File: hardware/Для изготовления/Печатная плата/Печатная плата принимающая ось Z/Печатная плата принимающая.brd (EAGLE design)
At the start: 30.4 x 29.2 mm, 6 parts, among them J1 22-03-5035, X1 0446200001

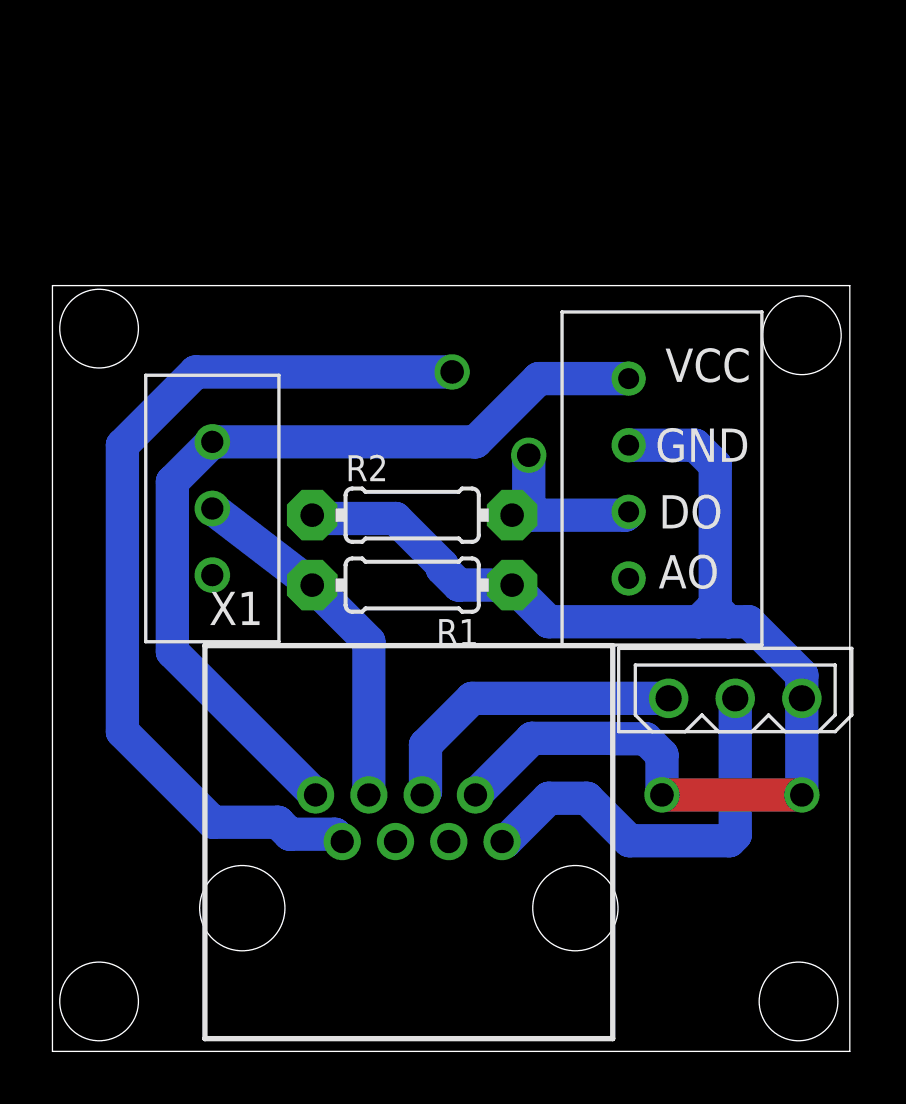
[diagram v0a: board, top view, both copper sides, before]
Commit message: Изменена плата принимающая под  ось Z
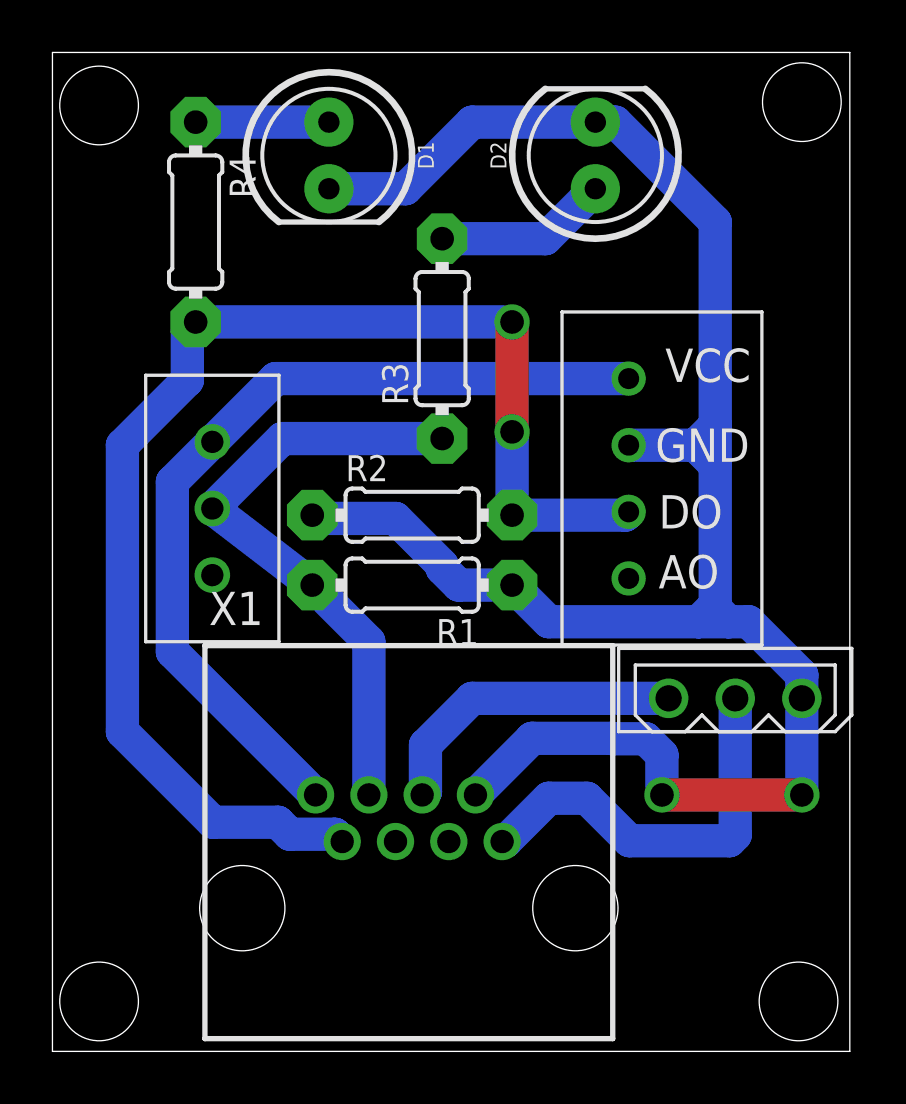
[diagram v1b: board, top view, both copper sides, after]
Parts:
- added D1, D2: (no value), SparkFun-LED:LED_5MM
- added R3, R4: (no value), resistor:0204/7
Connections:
- new net N$1: D2.A, R3.2
- new net N$2: D1.A, R4.1
- net ENCODER: now also R4.2
- net ENDSTOP: now also R3.1
- net GND: now also D1.K, D2.K
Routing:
- net GND: track 51.7 -> 79.4 mm
- net ENDSTOP: track 13.7 -> 23.6 mm
- net ENCODER: track 41.6 -> 50.8 mm
- net N$1: track 0.00 -> 6.63 mm
- net N$2: track 0.00 -> 5.08 mm
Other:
- board size 30.4 x 29.2 mm -> 30.4 x 38.1 mm
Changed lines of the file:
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@@
 <layer number="230" name="230bmp" color="7" fill="1" visible="yes" active="yes"/>
 <layer number="231" name="231bmp" color="7" fill="1" visible="yes" active="yes"/>
+<layer number="232" name="Eagle3D_PG2" color="7" fill="1" visible="yes" active="yes"/>
+<layer number="233" name="Eagle3D_PG3" color="7" fill="1" visible="yes" active="yes"/>
 <layer number="248" name="Housing" color="7" fill="1" visible="yes" active="yes"/>
 <layer number="249" name="Edge" color="7" fill="1" visible="yes" active="yes"/>
@@
 <plain>
 <wire x1="16.129" y1="-1.143" x2="46.533" y2="-1.143" width="0" layer="20"/>
-<wire x1="46.533" y1="-1.143" x2="46.533" y2="28.057" width="0" layer="20"/>
-<wire x1="46.533" y1="28.057" x2="16.129" y2="28.057" width="0" layer="20"/>
-<wire x1="16.129" y1="28.057" x2="16.129" y2="-1.143" width="0" layer="20"/>
-<hole x="17.907" y="26.416" drill="3"/>
+<wire x1="46.533" y1="-1.143" x2="46.533" y2="36.947" width="0" layer="20"/>
+<wire x1="46.533" y1="36.947" x2="16.129" y2="36.947" width="0" layer="20"/>
+<wire x1="16.129" y1="36.947" x2="16.129" y2="-1.143" width="0" layer="20"/>
+<hole x="17.907" y="34.925" drill="3"/>
 <hole x="17.907" y="0.762" drill="3"/>
 <hole x="44.577" y="0.762" drill="3"/>
-<hole x="44.704" y="26.162" drill="3"/>
+<hole x="44.704" y="35.052" drill="3"/>
 </plain>
 <attributes>
@@
 <attribute name="OC_FARNELL" value="unknown" x="29.718" y="4.318" size="1.778" layer="27" display="off"/>
 </element>
+<element name="D1" library="SparkFun-LED" package="LED_5MM" value="" x="26.67" y="33.02" rot="R270"/>
+<element name="D2" library="SparkFun-LED" package="LED_5MM" value="" x="36.83" y="33.02" rot="R90"/>
+<element name="R3" library="resistor" library_urn="urn:adsk.eagle:library:348" package="0204/7" package3d_urn="urn:adsk.eagle:package:25945/1" value="" x="30.988" y="26.035" rot="R90"/>
+<element name="R4" library="resistor" library_urn="urn:adsk.eagle:library:348" package="0204/7" package3d_urn="urn:adsk.eagle:package:25945/1" value="" x="21.59" y="30.48" rot="R270"/>
 </elements>
 <signals>
@@
 <contactref element="U$1" pad="VCC"/>
 <contactref element="U$2" pad="NC"/>
-<wire x1="38.1" y1="24.511" x2="34.671" y2="24.511" width="1.27" layer="16"/>
-<wire x1="32.258" y1="22.098" x2="22.225" y2="22.098" width="1.27" layer="16"/>
-<wire x1="34.671" y1="24.511" x2="32.258" y2="22.098" width="1.27" layer="16"/>
 <contactref element="X1" pad="8"/>
 <wire x1="22.225" y1="22.098" x2="20.701" y2="20.574" width="1.27" layer="16"/>
 <wire x1="20.701" y1="14.097" x2="26.162" y2="8.636" width="1.27" layer="16"/>
 <wire x1="20.701" y1="20.574" x2="20.701" y2="14.097" width="1.27" layer="16"/>
+<wire x1="22.225" y1="22.098" x2="24.638" y2="24.511" width="1.27" layer="16"/>
+<wire x1="24.638" y1="24.511" x2="38.1" y2="24.511" width="1.27" layer="16"/>
 </signal>
 <signal name="GND">
@@
 <wire x1="37.4824" y1="10.7776" x2="38.7524" y2="10.7776" width="1.27" layer="16"/>
 <wire x1="38.7524" y1="10.7776" x2="39.37" y2="10.16" width="1.27" layer="16"/>
+<contactref element="D2" pad="K"/>
+<contactref element="D1" pad="K"/>
+<wire x1="41.402" y1="30.48" x2="41.402" y2="22.733" width="1.27" layer="16"/>
+<wire x1="41.402" y1="22.733" x2="41.402" y2="21.209" width="1.27" layer="16"/>
+<wire x1="40.64" y1="21.971" x2="41.402" y2="22.733" width="1.27" layer="16"/>
+<wire x1="29.591" y1="31.75" x2="26.67" y2="31.75" width="1.27" layer="16"/>
+<wire x1="36.83" y1="34.29" x2="32.131" y2="34.29" width="1.27" layer="16"/>
+<wire x1="32.131" y1="34.29" x2="29.591" y2="31.75" width="1.27" layer="16"/>
+<wire x1="36.83" y1="34.29" x2="37.592" y2="34.29" width="1.27" layer="16"/>
+<wire x1="37.592" y1="34.29" x2="41.402" y2="30.48" width="1.27" layer="16"/>
 </signal>
 <signal name="RX/TX">
@@
 <contactref element="U$1" pad="DO"/>
 <contactref element="R2" pad="2"/>
-<wire x1="33.655" y1="19.304" x2="34.29" y2="19.304" width="1.27" layer="16"/>
-<wire x1="34.29" y1="19.304" x2="37.973" y2="19.304" width="1.27" layer="16"/>
+<wire x1="33.655" y1="19.304" x2="37.973" y2="19.304" width="1.27" layer="16"/>
 <wire x1="37.973" y1="19.304" x2="38.1" y2="19.431" width="1.27" layer="16"/>
 <contactref element="X1" pad="7"/>
-<via x="34.29" y="21.59" extent="1-16" drill="0.9"/>
-<wire x1="34.29" y1="21.59" x2="34.29" y2="19.304" width="1.27" layer="16"/>
-<wire x1="21.59" y1="24.765" x2="18.796" y2="21.971" width="1.27" layer="16"/>
-<via x="31.369" y="24.765" extent="1-16" drill="0.9"/>
-<wire x1="21.59" y1="24.765" x2="31.369" y2="24.765" width="1.27" layer="16"/>
+<wire x1="21.2725" y1="24.4475" x2="18.796" y2="21.971" width="1.27" layer="16"/>
 <wire x1="18.796" y1="21.971" x2="18.796" y2="11.049" width="1.27" layer="16"/>
 <wire x1="27.178" y1="6.858" x2="26.8986" y2="7.1374" width="1.27" layer="16"/>
@@
 <wire x1="22.2504" y1="7.5946" x2="24.7252125" y2="7.5946" width="1.27" layer="16"/>
 <wire x1="18.796" y1="11.049" x2="22.2504" y2="7.5946" width="1.27" layer="16"/>
-<wire x1="31.369" y1="24.765" x2="34.29" y2="21.59" width="0" layer="19" extent="1-1"/>
+<contactref element="R4" pad="2"/>
+<wire x1="21.59" y1="26.67" x2="21.2725" y2="26.3525" width="1.27" layer="16"/>
+<wire x1="21.2725" y1="26.3525" x2="21.2725" y2="24.4475" width="1.27" layer="16"/>
+<via x="33.655" y="26.67" extent="1-16" drill="0.9"/>
+<via x="33.655" y="22.479" extent="1-16" drill="0.9"/>
+<wire x1="21.59" y1="26.67" x2="33.655" y2="26.67" width="1.27" layer="16"/>
+<wire x1="33.655" y1="22.479" x2="33.655" y2="19.304" width="1.27" layer="16"/>
+<wire x1="33.655" y1="26.67" x2="33.655" y2="22.479" width="1.27" layer="1"/>
 </signal>
 <signal name="ENDSTOP">
@@
 <wire x1="28.194" y1="14.478" x2="28.194" y2="8.89" width="1.27" layer="16"/>
 <wire x1="22.225" y1="19.558" x2="26.035" y2="16.637" width="1.27" layer="16"/>
+<contactref element="R3" pad="1"/>
+<wire x1="22.225" y1="19.558" x2="24.892" y2="22.225" width="1.27" layer="16"/>
+<wire x1="24.892" y1="22.225" x2="30.988" y2="22.225" width="1.27" layer="16"/>
+</signal>
+<signal name="N$1">
+<contactref element="R3" pad="2"/>
+<contactref element="D2" pad="A"/>
+<wire x1="30.988" y1="29.845" x2="34.925" y2="29.845" width="1.27" layer="16"/>
+<wire x1="34.925" y1="29.845" x2="36.83" y2="31.75" width="1.27" layer="16"/>
+</signal>
+<signal name="N$2">
+<contactref element="R4" pad="1"/>
+<contactref element="D1" pad="A"/>
+<wire x1="21.59" y1="34.29" x2="26.67" y2="34.29" width="1.27" layer="16"/>
 </signal>
 </signals>
